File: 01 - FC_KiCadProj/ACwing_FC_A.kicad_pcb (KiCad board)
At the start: 4 copper layers, 40.8 x 40.8 mm, 110 parts, among them J1 USB-C (HRO TYPE-C-31-M-12), J2 ESC link, J3 Qwiic, J4 Qwiic, J5 ELRS, J6 ESC link B, J7 VBAT+, J8 GND, Q5 AO3401A, U1 LSM6DSV16X, U10 W25Q128JV, U11 LDK130PU-R, U12 LM5166DRCT, U2 STM32WB55CGU6, U3 IIS2MDC, U4 LPS22HB, U5 LD39130SPUR, U7 USBLC6-2SC6, U8 MLPF-WB55-01E3, Y1 32MHz

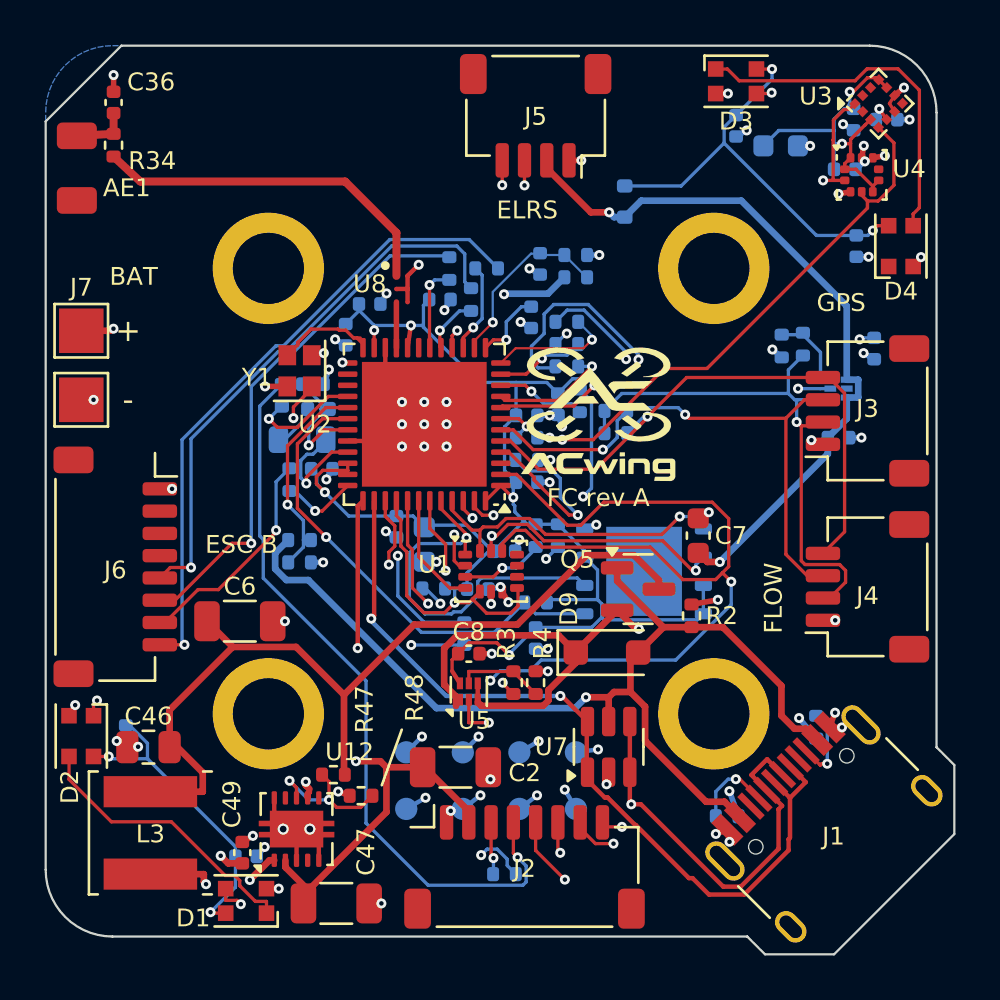
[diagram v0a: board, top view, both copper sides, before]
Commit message: FC/GPS layout update (still rev A): MCU centred, J6 on the front edge, buck on the left edge, EMI fixes
- FC: MCU at the board centre, IMU south of it (rot 270, axes remapped in firmware), ESC link B J6 next to J5 on
  the front edge, input buck L3/U12 on the left edge (out of the corner between the rear LEDs)
- FC: LEDs D3/D4 rotated, LED supply pre-routed away from the magnetometer; EMI check script and results
- GPS: Qwiic J1 moved to v = +3.6, right above FC J3
- re-routed, DRC 0 on both boards; Gerber, STEP, PDF, BoM/CPL, views, stack check regenerated; docs updated

Co-Authored-By: Claude Opus 5.5 <noreply@anthropic.com>
Claude-Session: https://claude.ai/code/session_0189Xg6tRAL4bRZ656VQBtPX
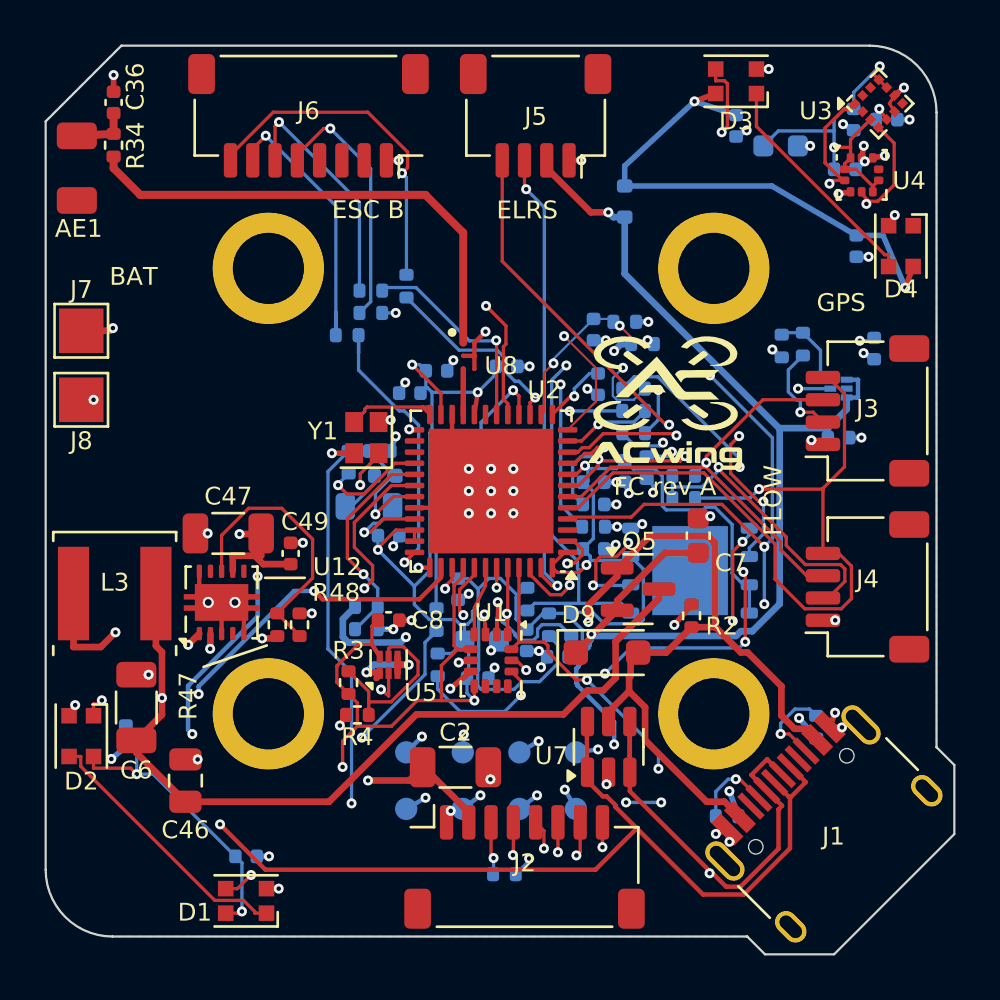
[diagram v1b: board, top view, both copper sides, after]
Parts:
- LOGO2: value ACwing_Logo_Full_5mm -> ACwing_Logo_Full_7mm; footprint ACwing:ACwing_Logo_Full_5mm -> ACwing:ACwing_Logo_Full_7mm
- moved J6 22.0 mm to (141.8, 83.2), turned to 180 degrees
- moved LOGO2 20.2 mm to (136.7, 102.3)
- moved C47 17.3 mm to (138.2, 101.9), turned to 180 degrees
- moved C49 13.6 mm to (141.0, 102.8)
- moved L3 10.9 mm to (133.1, 104.6), turned to 0 degrees
- moved U12 10.7 mm to (137.9, 105.0)
- moved R48 8.16 mm to (141.4, 106.0), turned to 90 degrees
- moved R4 8.13 mm to (144.0, 110.1), turned to 180 degrees
- moved R3 7.40 mm to (143.6, 108.6)
- moved R47 7.19 mm to (140.4, 106.0), turned to 90 degrees
- moved R27 6.98 mm to (143.5, 93.0), turned to 0 degrees
- moved C6 6.05 mm to (134.1, 109.7), turned to 90 degrees
- moved C9 5.04 mm to (149.6, 106.7), turned to 0 degrees
- moved R25 4.54 mm to (144.6, 92.0), turned to 0 degrees
- moved C1 4.24 mm to (154.8, 95.2)
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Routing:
- net BOOT0: track 20.9 -> 55.0 mm, vias 2 -> 7
- net IMU_CS: track 45.3 -> 18.7 mm, vias 3 -> 2
- net USB_DP: track 37.0 -> 61.9 mm, vias 2 -> 3
- net SPI_SCK: track 17.8 -> 42.0 mm, vias 3 -> 4
- net USB_DM: track 46.7 -> 68.1 mm, vias 2 -> 4
- net ESC_M3: track 26.9 -> 45.5 mm
- net FLASH_CS: track 21.6 -> 38.8 mm, vias 1 -> 2
- net VSYS: track 58.3 -> 73.6 mm, vias 3 -> 5
- net ESC_M5: track 25.1 -> 11.5 mm
- net ESC_M8: track 28.8 -> 15.4 mm
- net VBAT: track 75.4 -> 62.1 mm
- net ESC_M1: track 38.4 -> 25.5 mm
- net ESC_M6: track 23.6 -> 10.9 mm
- net SPI_MOSI: track 14.1 -> 26.2 mm, vias 1 -> 4
- net NRST: track 21.3 -> 31.8 mm, vias 2 -> 6
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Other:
- board text removed: "+"
- board text removed: "-"

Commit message: FC BoM fixes: R40 LCSC number, LPS22HH barometer, MCU sourcing note
- R40 47k 0402: C25819 (0603) -> C25792 (0402WGF4702TCE)
- U4: LPS22HBTR (out of stock) -> LPS22HHTR C2827824, same HLGA-10 footprint and pinout
- U2 STM32WB55CGU6 out of stock at LCSC/JLC: consigned part / Global Sourcing note

Co-Authored-By: Claude Opus 5.5 <noreply@anthropic.com>
Claude-Session: https://claude.ai/code/session_0189Xg6tRAL4bRZ656VQBtPX
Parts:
- U4: value LPS22HB -> LPS22HH
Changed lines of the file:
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@@
         (effects (font (size 0.8 0.8) (thickness 0.15)))
     )
-    (fp_text value "LPS22HB" (at 0 1.95) (layer "F.Fab")
+    (fp_text value "LPS22HH" (at 0 1.95) (layer "F.Fab")
         (effects (font (size 1 1) (thickness 0.15)))
     )

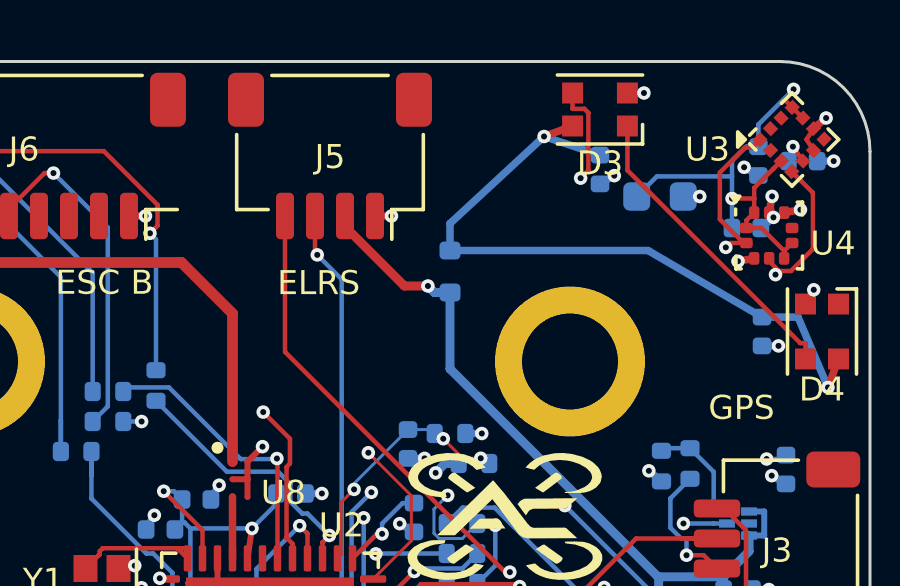
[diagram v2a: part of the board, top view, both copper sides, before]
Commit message: FC: XL-2020RGBC-WS2812B LEDs, D11 Schottky replaced by 0R link R49
- D1-D4: XINGLIGHT XL-2020RGBC-WS2812B (C5349955), same footprint and pinout (WS2812B-2020 out of stock)
- D11 RB521S30 -> R49 0R 0402 at the same place: VLED = VSYS, LEDs above their 3.5 V minimum on 1S
- BoM, JLC BoM, CPL, schematic PDF, Gerber, STEP, PCB view regenerated; DRC 0

Co-Authored-By: Claude Opus 5.5 <noreply@anthropic.com>
Claude-Session: https://claude.ai/code/session_0189Xg6tRAL4bRZ656VQBtPX
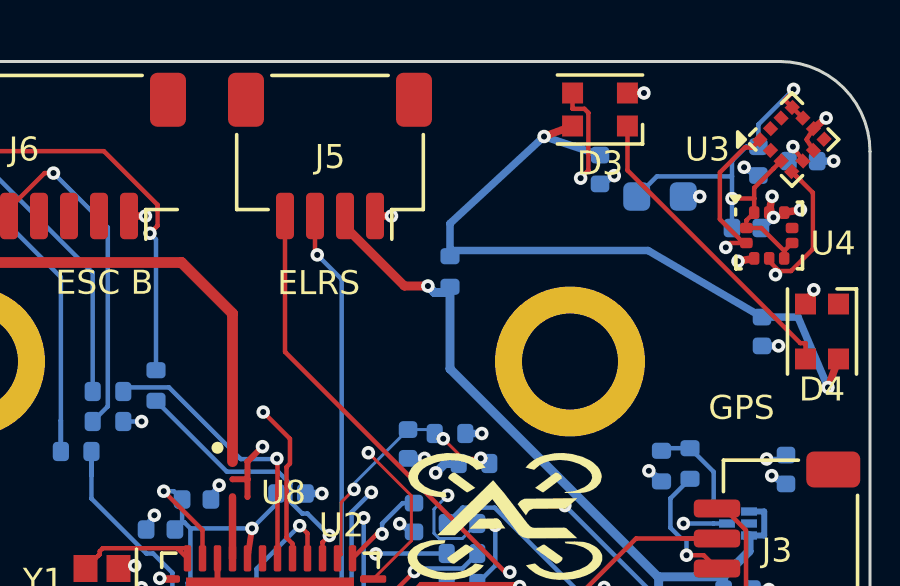
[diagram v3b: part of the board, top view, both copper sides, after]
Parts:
- removed D11: RB521S30, ACwing:D_SOD-523
- added R49: 0R, ACwing:R_0402_1005Metric, B.Cu at (156.0, 87.0)
- D1, D2, D3, D4: value WS2812B-2020 -> XL-2020RGBC-WS2812B
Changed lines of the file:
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@@
         (effects (font (size 0.8 0.8) (thickness 0.15)))
     )
-    (fp_text value "WS2812B-2020" (at 0 2.2 180) (layer "F.Fab")
+    (fp_text value "XL-2020RGBC-WS2812B" (at 0 2.2 180) (layer "F.Fab")
         (effects (font (size 1 1) (thickness 0.15)))
     )
@@
         (effects (font (size 0.8 0.8) (thickness 0.15)))
     )
-    (fp_text value "WS2812B-2020" (at 0 2.2 -90) (layer "F.Fab")
+    (fp_text value "XL-2020RGBC-WS2812B" (at 0 2.2 -90) (layer "F.Fab")
         (effects (font (size 1 1) (thickness 0.15)))
     )
@@
         (effects (font (size 0.8 0.8) (thickness 0.15)))
     )
-    (fp_text value "WS2812B-2020" (at 0 2.2 180) (layer "F.Fab")
+    (fp_text value "XL-2020RGBC-WS2812B" (at 0 2.2 180) (layer "F.Fab")
         (effects (font (size 1 1) (thickness 0.15)))
     )
@@
         (effects (font (size 0.8 0.8) (thickness 0.15)))
     )
-    (fp_text value "WS2812B-2020" (at 0 2.2 -90) (layer "F.Fab")
+    (fp_text value "XL-2020RGBC-WS2812B" (at 0 2.2 -90) (layer "F.Fab")
         (effects (font (size 1 1) (thickness 0.15)))
     )
@@
     )
   )
+  (footprint "ACwing:R_0402_1005Metric" (layer "B.Cu")
+    (at 156 87 90)
+    (descr "Resistor SMD 0402 (1005 Metric), square (rectangular) end terminal, IPC_7351 nominal, (Body size source: IPC-SM-782 page 72, https://www.pcb-3d.com/wordpress/wp-content/uploads/ipc-sm-782a_amendment_1_and_2.pdf), generated with kicad-footprint-generator")
+    (tags "resistor")
+    (attr smd)
+    (fp_text reference "R49" (at 0.6 1.6 90 unlocked) (layer "B.SilkS")
+        (effects (font (size 0.8 0.8) (thickness 0.15)) (justify mirror))
+    )
+    (fp_text value "0R" (at 0 -1.17 270) (layer "B.Fab")
+        (effects (font (size 1 1) (thickness 0.15)) (justify mirror))
+    )
+    (fp_text user "${REFERENCE}" (at 0 0 270) (layer "B.Fab")
+        (effects (font (size 0.26 0.26) (thickness 0.04)) (justify mirror))
+    )
+    (fp_line (start -0.153641 -0.38) (end 0.153641 -0.38)
+      (stroke (width 0.12) (type solid)) (layer "B.SilkS"))
+    (fp_line (start -0.153641 0.38) (end 0.153641 0.38)
+      (stroke (width 0.12) (type solid)) (layer "B.SilkS"))
+    (fp_line (start -0.93 -0.47) (end -0.93 0.47)
+      (stroke (width 0.05) (type solid)) (layer "B.CrtYd"))
+    (fp_line (start -0.93 0.47) (end 0.93 0.47)
+      (stroke (width 0.05) (type solid)) (layer "B.CrtYd"))
+    (fp_line (start 0.93 -0.47) (end -0.93 -0.47)
+      (stroke (width 0.05) (type solid)) (layer "B.CrtYd"))
+    (fp_line (start 0.93 0.47) (end 0.93 -0.47)
+      (stroke (width 0.05) (type solid)) (layer "B.CrtYd"))
+    (fp_line (start -0.525 -0.27) (end -0.525 0.27)
+      (stroke (width 0.1) (type solid)) (layer "B.Fab"))
+    (fp_line (start -0.525 0.27) (end 0.525 0.27)
+      (stroke (width 0.1) (type solid)) (layer "B.Fab"))
+    (fp_line (start 0.525 -0.27) (end -0.525 -0.27)
+      (stroke (width 0.1) (type solid)) (layer "B.Fab"))
+    (fp_line (start 0.525 0.27) (end 0.525 -0.27)
+      (stroke (width 0.1) (type solid)) (layer "B.Fab"))
+    (pad "1" smd roundrect (at -0.51 0 90) (size 0.54 0.64) (layers "B.Cu" "B.Paste" "B.Mask") (roundrect_rratio 0.25)
+      (net 68 "VSYS"))
+    (pad "2" smd roundrect (at 0.51 0 90) (size 0.54 0.64) (layers "B.Cu" "B.Paste" "B.Mask") (roundrect_rratio 0.25)
+      (net 53 "VLED"))
+    (model "${KIPRJMOD}/3d/R_0402_1005Metric.step"
+      (offset (xyz 0 0 0))
+      (scale (xyz 1 1 1))
+      (rotate (xyz 0 0 0))
+    )
+  )
   (footprint "ACwing:C_0603_1608Metric" (layer "B.Cu")
     (at 163 84.5)
@@
       (offset (xyz 0 0 0))
       (scale (xyz 1 1 1))
-      (rotate (xyz 0 0 0))
-    )
-  )
-  (footprint "ACwing:D_SOD-523" (layer "B.Cu")
-    (at 156 87 -90)
-    (descr "http://www.diodes.com/datasheets/ap02001.pdf p.144")
-    (tags "Diode SOD523")
-    (attr smd)
-    (fp_text reference "D11" (at 1.765 0 unlocked) (layer "B.SilkS")
-        (effects (font (size 0.8 0.8) (thickness 0.15)) (justify mirror))
-    )
-    (fp_text value "RB521S30" (at 0 -1.4 90) (layer "B.Fab")
-        (effects (font (size 1 1) (thickness 0.15)) (justify mirror))
-    )
-    (fp_text user "${REFERENCE}" (at 0 1.3 90) (layer "B.Fab")
-        (effects (font (size 1 1) (thickness 0.15)) (justify mirror))
-    )
-    (fp_line (start -1.26 0.6) (end -1.26 -0.6)
-      (stroke (width 0.12) (type solid)) (layer "B.SilkS"))
-    (fp_line (start 0.7 -0.6) (end -1.26 -0.6)
-      (stroke (width 0.12) (type solid)) (layer "B.SilkS"))
-    (fp_line (start 0.7 0.6) (end -1.26 0.6)
-      (stroke (width 0.12) (type solid)) (layer "B.SilkS"))
-    (fp_line (start -1.25 -0.7) (end -1.25 0.7)
-      (stroke (width 0.05) (type solid)) (layer "B.CrtYd"))
-    (fp_line (start -1.25 0.7) (end 1.25 0.7)
-      (stroke (width 0.05) (type solid)) (layer "B.CrtYd"))
-    (fp_line (start 1.25 -0.7) (end -1.25 -0.7)
-      (stroke (width 0.05) (type solid)) (layer "B.CrtYd"))
-    (fp_line (start 1.25 0.7) (end 1.25 -0.7)
-      (stroke (width 0.05) (type solid)) (layer "B.CrtYd"))
-    (fp_line (start -0.65 -0.45) (end -0.65 0.45)
-      (stroke (width 0.1) (type solid)) (layer "B.Fab"))
-    (fp_line (start -0.65 0.45) (end 0.65 0.45)
-      (stroke (width 0.1) (type solid)) (layer "B.Fab"))
-    (fp_line (start -0.2 -0.2) (end -0.2 0.2)
-      (stroke (width 0.1) (type solid)) (layer "B.Fab"))
-    (fp_line (start -0.2 0) (end -0.35 0)
-      (stroke (width 0.1) (type solid)) (layer "B.Fab"))
-    (fp_line (start -0.2 0) (end 0.1 -0.2)
-      (stroke (width 0.1) (type solid)) (layer "B.Fab"))
-    (fp_line (start 0.1 -0.2) (end 0.1 0.2)
-      (stroke (width 0.1) (type solid)) (layer "B.Fab"))
-    (fp_line (start 0.1 0) (end 0.25 0)
-      (stroke (width 0.1) (type solid)) (layer "B.Fab"))
-    (fp_line (start 0.1 0.2) (end -0.2 0)
-      (stroke (width 0.1) (type solid)) (layer "B.Fab"))
-    (fp_line (start 0.65 -0.45) (end -0.65 -0.45)
-      (stroke (width 0.1) (type solid)) (layer "B.Fab"))
-    (fp_line (start 0.65 0.45) (end 0.65 -0.45)
-      (stroke (width 0.1) (type solid)) (layer "B.Fab"))
-    (pad "1" smd roundrect (at -0.7 0 90) (size 0.6 0.7) (layers "B.Cu" "B.Paste" "B.Mask") (roundrect_rratio 0.25)
-      (net 53 "VLED"))
-    (pad "2" smd roundrect (at 0.7 0 90) (size 0.6 0.7) (layers "B.Cu" "B.Paste" "B.Mask") (roundrect_rratio 0.25)
-      (net 68 "VSYS"))
-    (model "${KIPRJMOD}/3d/D_SOD-523.step"
-      (offset (xyz 0 0 0))
-      (scale (xyz 1 1 1))

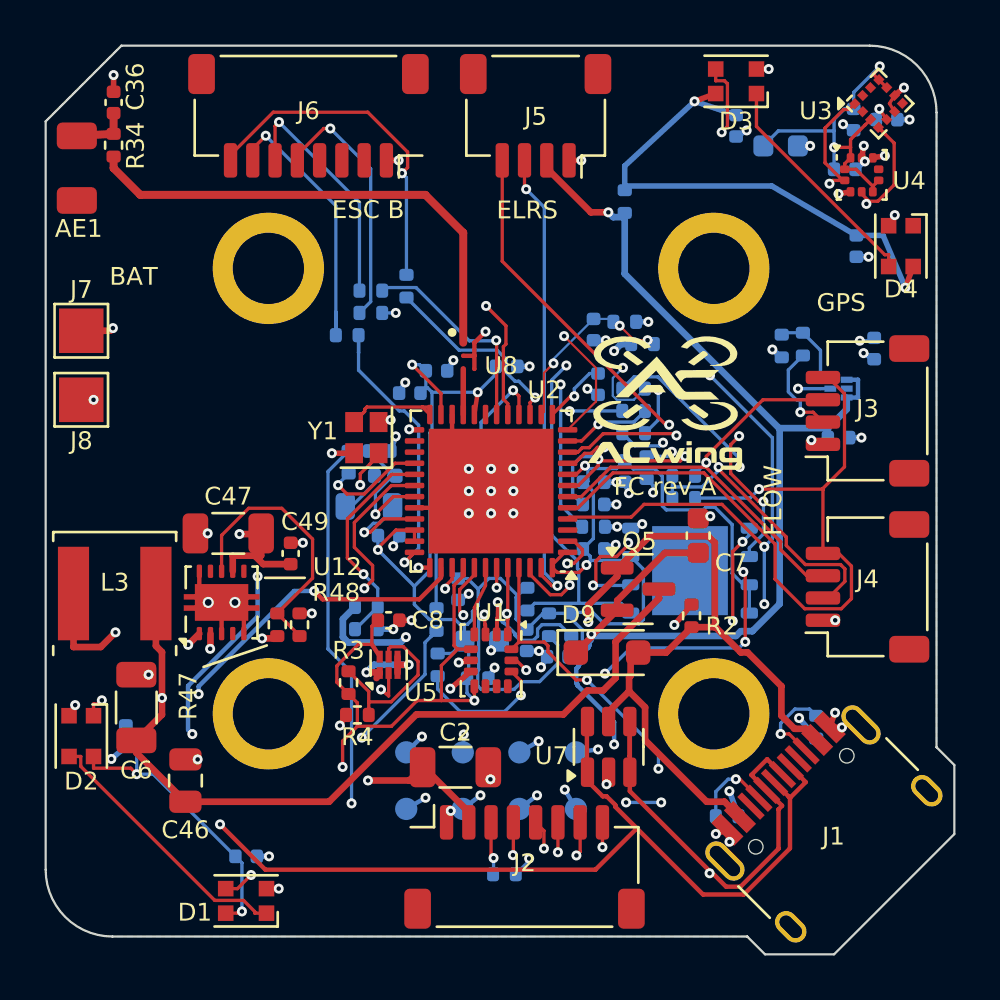
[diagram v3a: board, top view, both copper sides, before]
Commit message: FC rev A: LED data level shifter U13, LEDs on VSYS (R49 removed)
- U13 SN74LV1T34DCKR (TI, LCSC C78541, SC-70-5) single-supply buffer powered
  from VSYS: TTL-level input (VIH <= 2.0 V), push-pull output at VSYS, so the
  XL-2020RGBC-WS2812B data input (VIH = 0.7 x VDD) is met on battery and on
  USB alone. C50 100 nF decoupling; R39 33R between U13 and D1.
- R49 0R removed: VLED merged into VSYS (LED supply unchanged in geometry,
  EMI at the magnetometer unchanged).
- PCB: U13/C50/R39 on the bottom next to D1, RGB data rerouted; DRC 0
  violations, 0 unconnected.
- BoM/JLC BoM/CPL (U13 correction 270 deg), costing, schematic PDF, Gerber,
  STEP, views regenerated; README and pin map updated.

Co-Authored-By: Claude Opus 5.5 <noreply@anthropic.com>
Claude-Session: https://claude.ai/code/session_0189Xg6tRAL4bRZ656VQBtPX
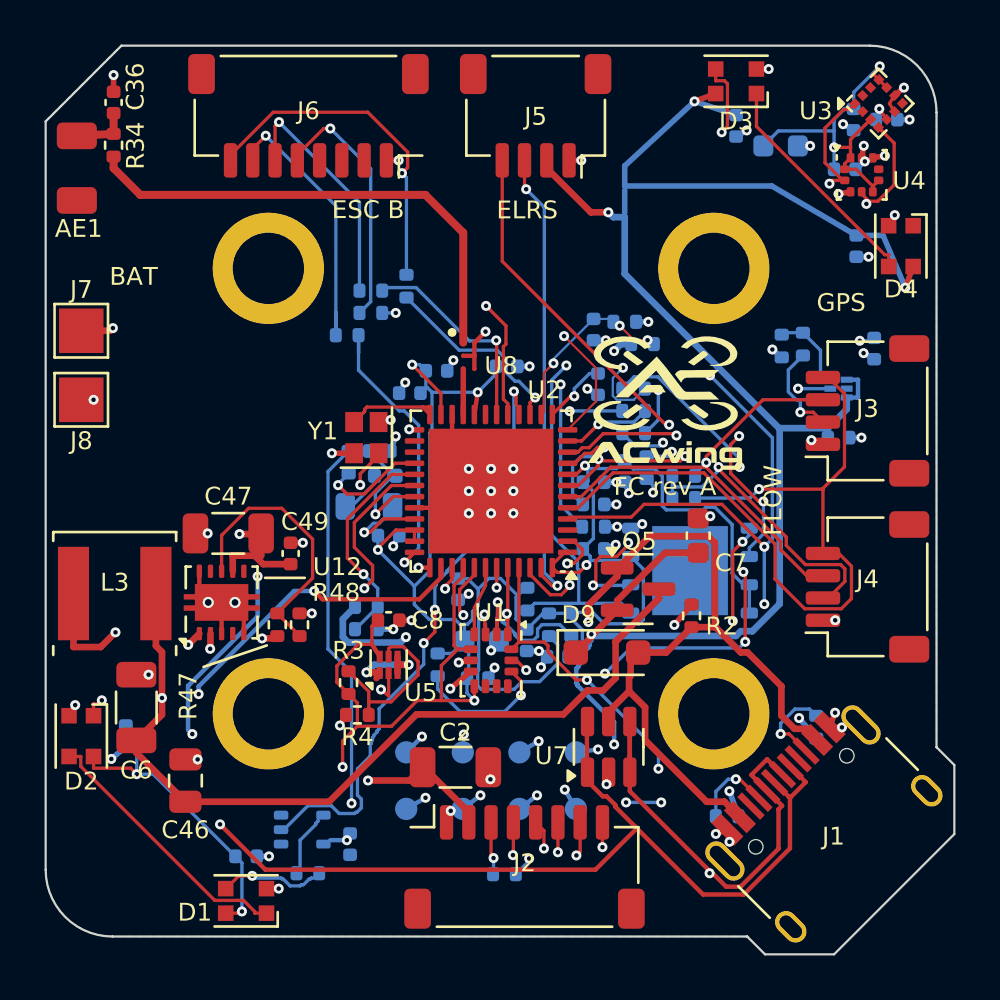
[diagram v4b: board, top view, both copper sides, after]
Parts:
- removed R49: 0R, ACwing:R_0402_1005Metric
- added C50: 100nF, ACwing:C_0402_1005Metric, B.Cu at (143.7, 115.8)
- added U13: SN74LV1T34DCKR, ACwing:SOT-353_SC-70-5, B.Cu at (141.5, 115.2)
- moved R39 12.8 mm to (141.8, 117.2), turned to 0 degrees
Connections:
- C40 pad 1: VLED -> VSYS
- C41 pad 1: VLED -> VSYS
- C42 pad 1: VLED -> VSYS
- C45 pad 1: VLED -> VSYS
- D1 pad 4: VLED -> VSYS
- D2 pad 4: VLED -> VSYS
- D3 pad 4: VLED -> VSYS
- D4 pad 4: VLED -> VSYS
- R39 pad 1: RGB_DIN -> RGB_DIN5
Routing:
- net VSYS: track 73.6 -> 165.3 mm, vias 5 -> 10
- net VLED: track 87.1 -> 0.00 mm, vias 4 -> 0
- net RGB_DIN: track 12.5 -> 26.2 mm, vias 1 -> 3
- net Net-(D1-DIN): track 16.6 -> 4.03 mm, vias 2 -> 1
- net RGB_DIN5: track 0.00 -> 2.38 mm
